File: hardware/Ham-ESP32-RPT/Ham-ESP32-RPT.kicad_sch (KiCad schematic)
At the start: 17 parts, among them J1 USB_C_Receptacle_USB2.0_16P, U1 ESP32-S3-WROOM-1, U2 D3V3XA4B10LP, U3 TLV75801PDBV

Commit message: Mise à jour documents
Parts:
- added J2: Conn_Coaxial, Connector_Coaxial:SMA_Molex_73251-1153_EdgeMount_Horizontal, symbol Connector:Conn_Coaxial
- added U4: ESP32-S3-DevKitC, PCM_Espressif:ESP32-S3-DevKitC, symbol PCM_Espressif:ESP32-S3-DevKitC
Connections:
- new net: U4.1 (3V3), U4.2 (3V3)
- new net: U4.22 (GND), U4.23 (GND), U4.24 (GND), U4.44 (GND)
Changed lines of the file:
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@@
+	)
+	(symbol
+		(lib_id "Connector:Conn_Coaxial")
+		(at 205.74 127 0)
+		(unit 1)
+		(exclude_from_sim no)
+		(in_bom yes)
+		(on_board yes)
+		(dnp no)
+		(fields_autoplaced yes)
+		(property "Reference" "J2"
+			(at 209.55 126.0231 0)
+			(effects
+				(font
+					(size 1.27 1.27)
+				)
+				(justify left)
+			)
+		)
+		(property "Value" "Conn_Coaxial"
+			(at 209.55 128.5631 0)
+			(effects
+				(font
+					(size 1.27 1.27)
+				)
+				(justify left)
+			)
+		)
+		(property "Footprint" "Connector_Coaxial:SMA_Molex_73251-1153_EdgeMount_Horizontal"
+			(at 205.74 127 0)
+			(effects
+				(font
+					(size 1.27 1.27)
+				)
+				(hide yes)
+			)
+		)
+		(property "Datasheet" "~"
+			(at 205.74 127 0)
+			(effects
+				(font
+					(size 1.27 1.27)
+				)
+				(hide yes)
+			)
+		)
+		(property "Description" "coaxial connector (BNC, SMA, SMB, SMC, Cinch/RCA, LEMO, ...)"
+			(at 205.74 127 0)
+			(effects
+				(font
+					(size 1.27 1.27)
+				)
+				(hide yes)
+			)
+		)
+		(pin "2"
+		)
+		(pin "1"
+		)
+		(instances
+			(project ""
+				(path "/1aedab51-3492-4fbd-b88f-5a8cb3ade46f"
+					(reference "J2")
+					(unit 1)
+				)
+			)
+		)
 	)
 	(symbol
@@
 					(unit 1)
 				)
+			)
+		)
+	)
+	(symbol
+		(lib_id "PCM_Espressif:ESP32-S3-DevKitC")
+		(at 251.46 104.14 0)
+		(unit 1)
+		(exclude_from_sim no)
+		(in_bom yes)
+		(on_board yes)
+		(dnp no)
+		(fields_autoplaced yes)
+		(property "Reference" "U4"
+			(at 253.6541 149.86 0)
+			(effects
+				(font
+					(size 1.27 1.27)
+				)
+				(justify left)
+			)
+		)
+		(property "Value" "ESP32-S3-DevKitC"
+			(at 253.6541 152.4 0)
+			(effects
+				(font
+					(size 1.27 1.27)
+				)
+				(justify left)
+			)
+		)
+		(property "Footprint" "PCM_Espressif:ESP32-S3-DevKitC"
+			(at 251.46 161.29 0)
+			(effects
+				(font
+					(size 1.27 1.27)
+				)
+				(hide yes)
+			)
+		)
+		(property "Datasheet" ""
+			(at 191.77 106.68 0)
+			(effects
+				(font
+					(size 1.27 1.27)
+				)
+				(hide yes)
+			)
+		)
+		(property "Description" "ESP32-S3-DevKitC"
+			(at 251.46 104.14 0)
+			(effects
+				(font
+					(size 1.27 1.27)
+				)
+				(hide yes)
+			)
+		)
+		(pin "14"
+		)
+		(pin "20"
+		)
+		(pin "11"
+		)
+		(pin "31"
+		)
+		(pin "38"
+		)
+		(pin "19"
+		)
+		(pin "39"
+		)
+		(pin "1"
+		)
+		(pin "42"
+		)
+		(pin "13"
+		)
+		(pin "21"
+		)
+		(pin "22"
+		)
+		(pin "32"
+		)
+		(pin "44"
+		)
+		(pin "25"
+		)
+		(pin "33"
+		)
+		(pin "26"
+		)
+		(pin "34"
+		)
+		(pin "35"
+		)
+		(pin "28"
+		)
+		(pin "36"
+		)
+		(pin "18"
+		)
+		(pin "3"
+		)
+		(pin "27"
+		)
+		(pin "2"
+		)
+		(pin "23"
+		)
+		(pin "17"
+		)
+		(pin "16"
+		)
+		(pin "37"
+		)
+		(pin "41"
+		)
+		(pin "5"
+		)
+		(pin "29"
+		)
+		(pin "6"
+		)
+		(pin "8"
+		)
+		(pin "24"
+		)
+		(pin "10"
+		)
+		(pin "43"
+		)
+		(pin "15"
+		)
+		(pin "40"
+		)
+		(pin "30"
+		)
+		(pin "7"
+		)
+		(pin "9"
+		)
+		(pin "12"
+		)
+		(pin "4"
+		)
+		(instances
+			(project ""
+				(path "/1aedab51-3492-4fbd-b88f-5a8cb3ade46f"
+					(reference "U4")
+					(unit 1)
+				)

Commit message: doc HAM-ESP32
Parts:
- removed BOOT1, RESET1: SW_MEC_5E, Button_Switch_SMD:SW_MEC_5GSH9, symbol PCM_Switch:SW_MEC_5E
- removed C1, C3, C4: 0.1µF, Capacitor_SMD:C_0805_2012Metric, symbol Device:C
- removed C2, C6, C7: 10µF, Capacitor_SMD:C_0805_2012Metric, symbol Device:C
- removed J1: USB_C_Receptacle_USB2.0_16P, Connector_USB:USB_C_Receptacle_GCT_USB4085, symbol Connector:USB_C_Receptacle_USB2.0_16P
- removed J2: Conn_Coaxial, Connector_Coaxial:SMA_Molex_73251-1153_EdgeMount_Horizontal, symbol Connector:Conn_Coaxial
- removed R3: 10k, Resistor_SMD:R_0805_2012Metric, symbol Device:R
- removed R6: 1M, Resistor_SMD:R_0805_2012Metric, symbol Device:R
- removed R7: 200k, Resistor_SMD:R_0805_2012Metric, symbol Device:R
- removed R8: 5.1K, Resistor_SMD:R_0805_2012Metric, symbol Device:R
- removed U1: ESP32-S3-WROOM-1, RF_Module:ESP32-S3-WROOM-1U, symbol RF_Module:ESP32-S3-WROOM-1
- removed U2: D3V3XA4B10LP, Package_DFN_QFN:Diodes_UDFN-10_1.0x2.5mm_P0.5mm, symbol Power_Protection:D3V3XA4B10LP
- removed U3: TLV75801PDBV, Package_TO_SOT_SMD:SOT-23-5, symbol Regulator_Linear:TLV75801PDBV
- added D1: GREEN, symbol Device:LED
- added J1: RSSI IN, symbol Connector:Conn_01x02_Pin
- added J2: AUDIO OUT, symbol Connector:Conn_01x02_Pin
- added J3: AUDIO IN, symbol Connector:Conn_01x02_Pin
- added J4: PTT OUT, symbol Connector:Conn_01x02_Pin
- added R1, R2: 330R, symbol Device:R
- added SW1: REP TEST, symbol Switch:SW_Push
- added U1: CS5343, Package_SO:TSSOP-10_3x3mm_P0.5mm, symbol Audio:CS5343
- added U2: CS4344, Package_SO:TSSOP-10_3x3mm_P0.5mm, symbol Audio:CS4344
- D2: value LED -> RED; footprint LED_SMD:LED_0805_2012Metric -> (none)
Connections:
- net GND: now also U4.22 (GND), U4.23 (GND), U4.24 (GND), U4.44 (GND), D1.1 (K), J1.2 (Pin_2), J2.2 (Pin_2), J3.2 (Pin_2), J4.2 (Pin_2), SW1.2, U1.9 (GND), U2.8 (GND)
- net at D2.2 (A): now also R2.2
- net VCC: now reaches U4.1 (3V3), U4.2 (3V3)
- net VCC: now also U1.10 (VA), U2.9 (VA)
- net at U4.12 (GPIO8/ADC1_CH7): now also J1.1 (Pin_1)
- net at U4.13 (GPIO3/ADC1_CH2): now also U1.1 (SDOUT)
- net at U4.15 (GPIO9/ADC1_CH8): now also R1.1
- net at U4.16 (GPIO10/ADC1_CH9): now also R2.1
- net at U4.17 (GPIO11/ADC2_CH0): now also SW1.1
- net at U4.18 (GPIO12/ADC2_CH1): now also J4.1 (Pin_1)
- net at U4.31 (GPIO0): now also U1.4 (MCLK)
- net at U4.4 (GPIO4/ADC1_CH3): now also U2.4 (MCLK)
- net at U4.40 (GPIO2/ADC1_CH1): now also U1.2 (SCLK)
- net at U4.41 (GPIO1/ADC1_CH0): now also U1.3 (LRCK)
- net at U4.5 (GPIO5/ADC1_CH4): now also U2.3 (LRCK)
- net at U4.6 (GPIO6/ADC1_CH5): now also U2.2 (~{DEM}/SCLK)
- net at U4.7 (GPIO7/ADC1_CH6): now also U2.1 (SDIN)
- new net: J3.1 (Pin_1), U1.5 (FILT+)
- new net: J2.1 (Pin_1), U2.7 (AOUTL)
- new net: D1.2 (A), R1.2
- no-connect marks 2 -> 0
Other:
- moved on the sheet: U4

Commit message: Update Kicad Schematic
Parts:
- removed J1: RSSI IN, symbol Connector:Conn_01x02_Pin
- removed J2: AUDIO OUT, symbol Connector:Conn_01x02_Pin
- removed J3: AUDIO IN, symbol Connector:Conn_01x02_Pin
- removed J4: PTT OUT, symbol Connector:Conn_01x02_Pin
- removed U1: CS5343, Package_SO:TSSOP-10_3x3mm_P0.5mm, symbol Audio:CS5343
- removed U2: CS4344, Package_SO:TSSOP-10_3x3mm_P0.5mm, symbol Audio:CS4344
- added FB1: FerriteBead, Ferrite_THT:LairdTech_28C0236-0JW-10, symbol Device:FerriteBead
- added J5: Conn_01x04_Socket, Connector_JST:JST_XH_B4B-XH-A_1x04_P2.50mm_Vertical, symbol Connector:Conn_01x04_Socket
- added Q1: MMBT3904, Package_TO_SOT_SMD:SOT-23, symbol Transistor_BJT:MMBT3904
- D1, D2: footprint (none) -> LED_SMD:LED_1206_3216Metric
- R1, R2: footprint (none) -> Resistor_SMD:R_1206_3216Metric
- SW1: footprint (none) -> Button_Switch_THT:SW_PUSH_6mm

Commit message: PCB kicad update
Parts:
- removed J5: Conn_01x04_Socket, Connector_JST:JST_XH_B4B-XH-A_1x04_P2.50mm_Vertical, symbol Connector:Conn_01x04_Socket
- removed Q1: MMBT3904, Package_TO_SOT_SMD:SOT-23, symbol Transistor_BJT:MMBT3904
- removed SW1: REP TEST, Button_Switch_THT:SW_PUSH_6mm, symbol Switch:SW_Push
- removed U4: ESP32-S3-DevKitC, PCM_Espressif:ESP32-S3-DevKitC, symbol PCM_Espressif:ESP32-S3-DevKitC
- added D1: BLUE, LED_SMD:LED_1206_3216Metric, symbol Device:LED
- added F1: 2A, Fuse:Fuse_1206_3216Metric, symbol Device:Fuse
- added F2, F3: 4A, Fuse:Fuse_1206_3216Metric, symbol Device:Fuse
- added FB2, FB3, FB4: VK200, Inductor_SMD:L_Neosid_MicroCoil_Ms36-L, symbol Device:FerriteBead
- added J1: 5V SUPPLY, Connector_JST:JST_XH_B2B-XH-A_1x02_P2.50mm_Vertical, symbol Connector_Generic:Conn_01x02
- added J2: 12V SUPPLY, Connector_JST:JST_XH_B2B-XH-A_1x02_P2.50mm_Vertical, symbol Connector_Generic:Conn_01x02
- added J3: RX RADIO, Connector_JST:JST_XH_B5B-XH-A_1x05_P2.50mm_Vertical, symbol Connector_Generic:Conn_01x05
- added J4: TX RADIO, Connector_JST:JST_XH_B4B-XH-A_1x04_P2.50mm_Vertical, symbol Connector_Generic:Conn_01x04
- added J5: AUX BTN LED, Connector_JST:JST_XH_B5B-XH-A_1x05_P2.50mm_Vertical, symbol Connector_Generic:Conn_01x05
- added J6: SPEAKER, Connector_JST:JST_XH_B2B-XH-A_1x02_P2.50mm_Vertical, symbol Connector_Generic:Conn_01x02
- added Q1: MMBT2222A, Package_TO_SOT_SMD:TSOT-23, symbol Transistor_BJT:MMBT2222A
- added R1: 330R, Resistor_SMD:R_1206_3216Metric, symbol Device:R
- added R2: 3.3K, Resistor_SMD:R_1206_3216Metric, symbol Device:R
- added SW2: TEST, Button_Switch_SMD:SW_Push_1P1T_NO_E-Switch_TL3301NxxxxxG, symbol Switch:SW_Push
- added U1: ESP32-S3-DevKitC-V2, Ham-ESP32-RPT-pretty:ESP32-S3-DevKitC-V2, symbol Ham-ESP32-RPT:ESP32-S3-DevKitC-V2
- added U2: PmodI2S2, symbol Ham-ESP32-RPT:PmodI2S2
- added U3: INA219AxD, Package_SO:SOIC-8_3.9x4.9mm_P1.27mm, symbol Sensor_Energy:INA219AxD
- added VR1, VR2, VR3: 10K, Potentiometer_SMD:Potentiometer_Bourns_3314R-1_Vertical_Hole, symbol Device:R_Potentiometer
- FB1: value FerriteBead -> VK200; footprint Ferrite_THT:LairdTech_28C0236-0JW-10 -> Inductor_SMD:L_Neosid_MicroCoil_Ms36-L
- renumbered D1 to D3, R2 to R3, R1 to R4
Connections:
- net GND: now also J1.2 (Pin_2), J2.2 (Pin_2), J3.4 (Pin_4), J4.3 (Pin_3), Q1.2 (E), R1.2, SW2.2, U1.1 (GND), U1.42 (GND), U2.11 (GND), U2.14 (A_IN-), U2.16 (A_OUT-), U2.5 (GND), U3.6 (GND), VR1.1, VR2.3, VR3.1
- net at R4.1: now also U1.8 (G15)
- net at R3.1: now also U1.24 (G14)
- net at FB1.1: now also D1.2 (A), F1.2
- net +5V: now reaches FB1.2
- net +5V: now also U1.22 (5V)
- new net: R2.1, U1.20 (G12)
- new net: Q1.1 (B), R2.2
- new net: U2.13 (A_IN+), VR1.2
- new net: FB2.2, VR1.3
- new net: D1.1 (K), R1.1
- new net: FB4.1, J3.1 (Pin_1)
- new net: FB2.1, J3.2 (Pin_2)
- new net: F2.2, J3.5 (Pin_5)
- new net: F1.1, J1.1 (Pin_1)
- new net: U1.12 (G8), U3.3 (SDA)
- new net: U1.15 (G3), U2.4 (ADOUT_SDIN)
- new net: U1.17 (G9), U3.4 (SCL)
- new net: SW2.1, U1.19 (G11)
- new net: U1.29 (G0), U2.1 (ADOUT_MCLK)
- new net: U1.4 (G4), U2.7 (ADIN_MCLK)
- new net: U1.40 (G2), U2.3 (ADOUT_SCLK)
- new net: U1.41 (G1), U2.2 (ADOUT_LRCK)
- new net: U1.5 (G5), U2.8 (ADIN_LRCK)
- new net: U1.6 (G6), U2.9 (ADIN_SCLK)
- new net: U1.7 (G7), U2.10 (ADIN_SDOUT)
- new net: J4.1 (Pin_1), Q1.3 (C)
- new net: FB3.2, J4.2 (Pin_2)
- new net: F3.2, J4.4 (Pin_4)
- new net: U2.15 (A_OUT+), VR2.1
- new net: FB4.2, VR3.3
- new net: FB3.1, VR2.2
- new net: F2.1, F3.1, J2.1 (Pin_1)
- new net: U3.8 (IN+), VR3.2
- new net +3.3V: U1.2 (3V3), U1.21 (3V3), U2.12 (3V3), U2.6 (3V3), U3.5 (VS)
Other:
- moved on the sheet: D2, D3, FB1, R3, R4

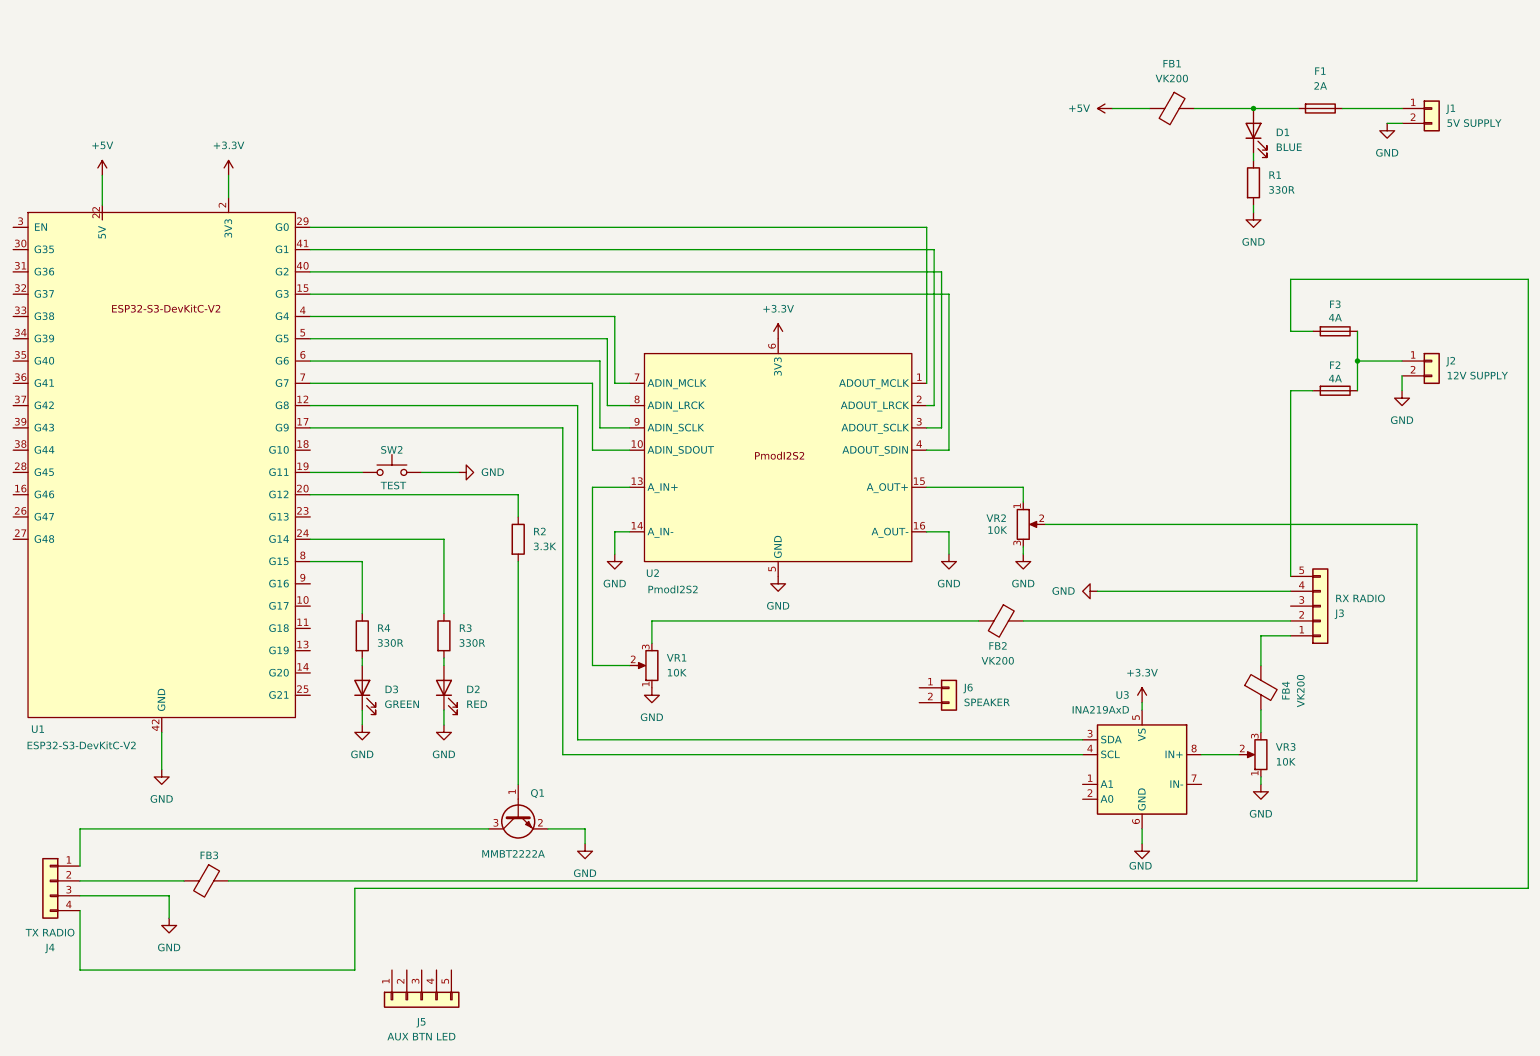
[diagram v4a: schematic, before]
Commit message: Add Vk200 footprint
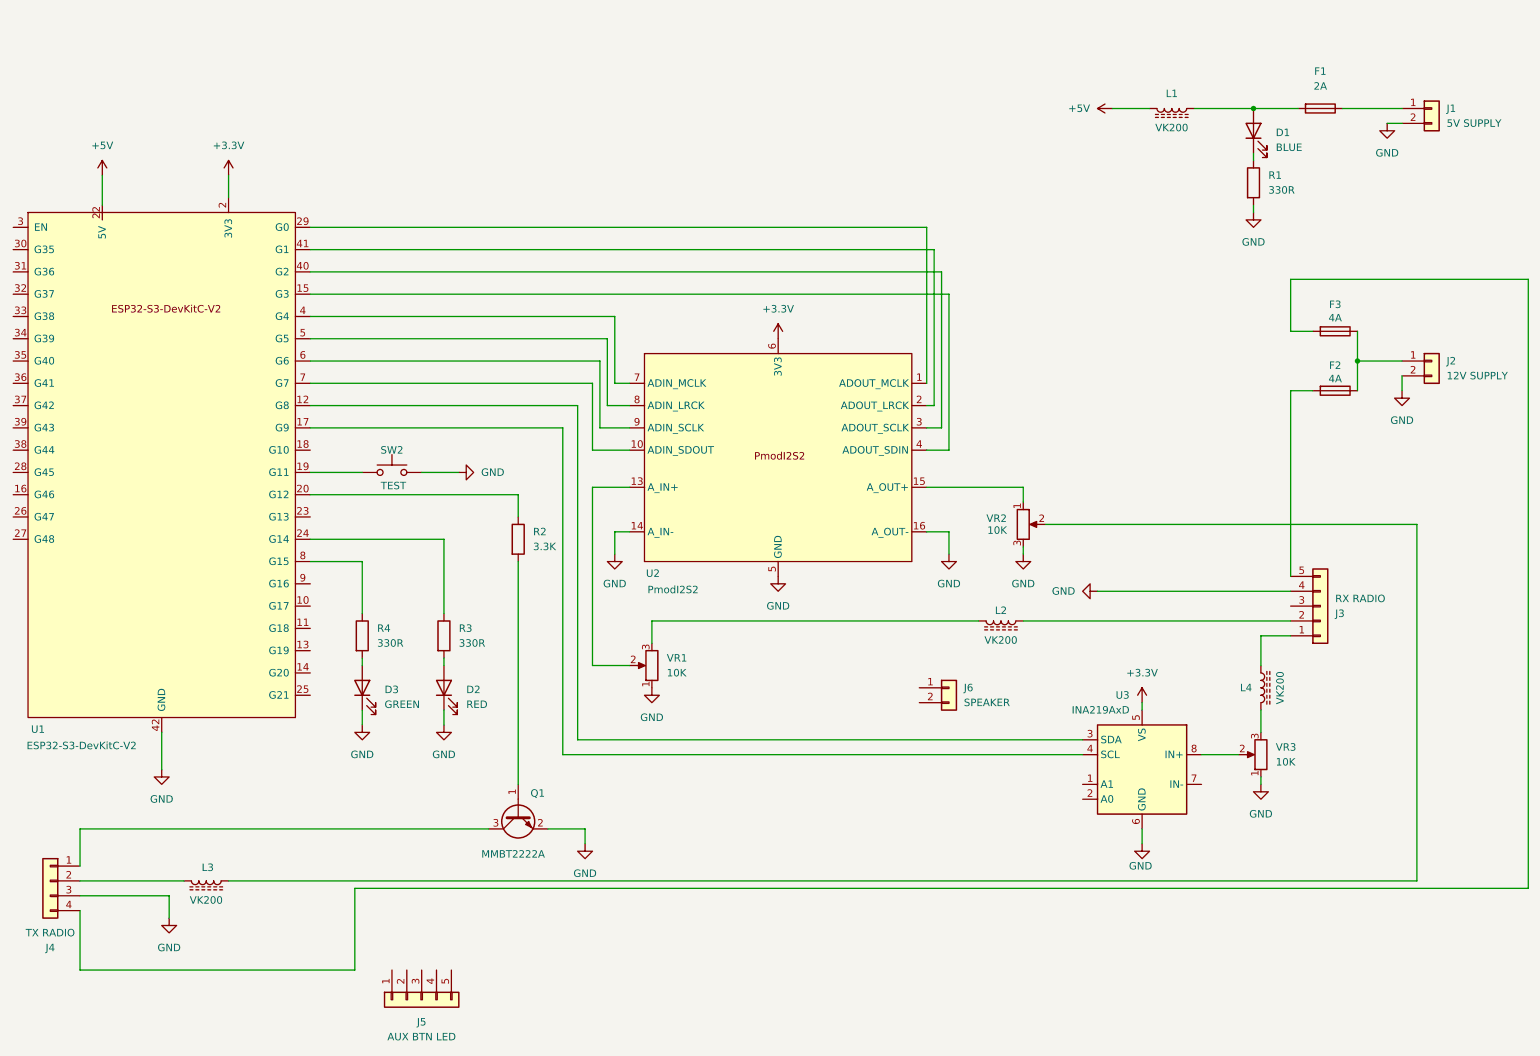
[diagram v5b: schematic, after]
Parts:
- L1: renamed from FB1; footprint Inductor_SMD:L_Neosid_MicroCoil_Ms36-L -> Ham-ESP32-RPT-pretty:VK200; symbol Device:FerriteBead -> Ham-ESP32-RPT:VK200
- L2: renamed from FB2; footprint Inductor_SMD:L_Neosid_MicroCoil_Ms36-L -> Ham-ESP32-RPT-pretty:VK200; symbol Device:FerriteBead -> Ham-ESP32-RPT:VK200
- L3: renamed from FB3; footprint Inductor_SMD:L_Neosid_MicroCoil_Ms36-L -> VK200; symbol Device:FerriteBead -> Ham-ESP32-RPT:VK200
- L4: renamed from FB4; footprint Inductor_SMD:L_Neosid_MicroCoil_Ms36-L -> Ham-ESP32-RPT-pretty:VK200; symbol Device:FerriteBead -> Ham-ESP32-RPT:VK200
- Q1: footprint Package_TO_SOT_SMD:TSOT-23 -> Package_TO_SOT_SMD:SOT-23
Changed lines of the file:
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@@
 	)
 	(symbol
-		(lib_id "Device:FerriteBead")
+		(lib_id "Ham-ESP32-RPT:VK200")
 		(at 236.22 129.54 0)
 		(unit 1)
@@
 		(on_board yes)
 		(dnp no)
-		(property "Reference" "FB4"
-			(at 240.538 130.048 90)
+		(property "Reference" "L4"
+			(at 233.68 129.54 0)
 			(effects
 				(font
@@
 		)
 		(property "Value" "VK200"
-			(at 243.078 130.048 90)
-			(effects
-				(font
-					(size 1.27 1.27)
-				)
-			)
-		)
-		(property "Footprint" "Inductor_SMD:L_Neosid_MicroCoil_Ms36-L"
-			(at 234.442 129.54 90)
+			(at 239.522 129.54 90)
+			(effects
+				(font
+					(size 1.27 1.27)
+				)
+			)
+		)
+		(property "Footprint" "Ham-ESP32-RPT-pretty:VK200"
+			(at 236.22 129.54 0)
 			(effects
 				(font
@@
 			)
 		)
-		(property "Description" "Ferrite bead"
+		(property "Description" "Inductor with ferrite core"
 			(at 236.22 129.54 0)
 			(effects
@@
 			(project "Ham-ESP32-RPT"
 				(path "/1aedab51-3492-4fbd-b88f-5a8cb3ade46f"
-					(reference "FB4")
+					(reference "L4")
 					(unit 1)
 				)
@@
 	)
 	(symbol
-		(lib_id "Device:FerriteBead")
+		(lib_id "Ham-ESP32-RPT:VK200")
 		(at 191.77 118.11 270)
 		(unit 1)
@@
 		(on_board yes)
 		(dnp no)
-		(property "Reference" "FB2"
-			(at 191.262 122.428 90)
+		(property "Reference" "L2"
+			(at 191.77 116.332 90)
 			(effects
 				(font
@@
 		)
 		(property "Value" "VK200"
-			(at 191.262 124.968 90)
-			(effects
-				(font
-					(size 1.27 1.27)
-				)
-			)
-		)
-		(property "Footprint" "Inductor_SMD:L_Neosid_MicroCoil_Ms36-L"
-			(at 191.77 116.332 90)
+			(at 191.77 121.412 90)
+			(effects
+				(font
+					(size 1.27 1.27)
+				)
+			)
+		)
+		(property "Footprint" "Ham-ESP32-RPT-pretty:VK200"
+			(at 191.77 118.11 0)
 			(effects
 				(font
@@
 			)
 		)
-		(property "Description" "Ferrite bead"
+		(property "Description" "Inductor with ferrite core"
 			(at 191.77 118.11 0)
 			(effects
@@
 			(project "Ham-ESP32-RPT"
 				(path "/1aedab51-3492-4fbd-b88f-5a8cb3ade46f"
-					(reference "FB2")
+					(reference "L2")
 					(unit 1)
 				)
@@
 	)
 	(symbol
-		(lib_id "Device:FerriteBead")
+		(lib_id "Ham-ESP32-RPT:VK200")
 		(at 55.88 162.56 270)
 		(unit 1)
@@
 		(on_board yes)
 		(dnp no)
-		(property "Reference" "FB3"
-			(at 56.388 158.242 90)
+		(property "Reference" "L3"
+			(at 56.134 160.274 90)
 			(effects
 				(font
@@
 		)
 		(property "Value" "VK200"
-			(at 56.896 156.21 90)
-			(effects
-				(font
-					(size 1.27 1.27)
-				)
-				(hide yes)
-			)
-		)
-		(property "Footprint" "Inductor_SMD:L_Neosid_MicroCoil_Ms36-L"
-			(at 55.88 160.782 90)
+			(at 55.88 165.862 90)
+			(effects
+				(font
+					(size 1.27 1.27)
+				)
+			)
+		)
+		(property "Footprint" "VK200"
+			(at 55.88 162.56 0)
 			(effects
 				(font
@@
 			)
 		)
-		(property "Description" "Ferrite bead"
+		(property "Description" "Inductor with ferrite core"
 			(at 55.88 162.56 0)
 			(effects
@@
 			(project "Ham-ESP32-RPT"
 				(path "/1aedab51-3492-4fbd-b88f-5a8cb3ade46f"
-					(reference "FB3")
+					(reference "L3")
 					(unit 1)
 				)
@@
 			)
 		)
-		(property "Footprint" "Package_TO_SOT_SMD:TSOT-23"
+		(property "Footprint" "Package_TO_SOT_SMD:SOT-23"
 			(at 111.125 156.21 0)
 			(effects
@@
 		)
 		(property "Description" "600mA Ic, 40V Vce, NPN Transistor, SOT-23"
+			(at 109.22 151.13 0)
+			(effects
+				(font
+					(size 1.27 1.27)
+				)
+				(hide yes)
+			)
+		)
+		(property "Sim.Device" "NPN"
+			(at 109.22 151.13 0)
+			(effects
+				(font
+					(size 1.27 1.27)
+				)
+				(hide yes)
+			)
+		)
+		(property "Sim.Pins" "1=B 2=E 3=C"
 			(at 109.22 151.13 0)
 			(effects
@@
 	)
 	(symbol
-		(lib_id "Device:FerriteBead")
+		(lib_id "Ham-ESP32-RPT:VK200")
 		(at 220.98 30.48 270)
 		(unit 1)
@@
 		(on_board yes)
 		(dnp no)
-		(fields_autoplaced yes)
-		(property "Reference" "FB1"
-			(at 221.0308 22.86 90)
+		(property "Reference" "L1"
+			(at 220.98 27.94 90)
 			(effects
 				(font
@@
 		)
 		(property "Value" "VK200"
-			(at 221.0308 25.4 90)
-			(effects
-				(font
-					(size 1.27 1.27)
-				)
-			)
-		)
-		(property "Footprint" "Inductor_SMD:L_Neosid_MicroCoil_Ms36-L"
-			(at 220.98 28.702 90)
+			(at 220.98 33.782 90)
+			(effects
+				(font
+					(size 1.27 1.27)
+				)
+			)
+		)
+		(property "Footprint" "Ham-ESP32-RPT-pretty:VK200"
+			(at 220.98 30.48 0)
 			(effects
 				(font
@@
 			)
 		)
-		(property "Description" "Ferrite bead"
+		(property "Description" "Inductor with ferrite core"
 			(at 220.98 30.48 0)
 			(effects
@@
 			(project ""
 				(path "/1aedab51-3492-4fbd-b88f-5a8cb3ade46f"
-					(reference "FB1")
-					(unit 1)
-				)
+					(reference "L1")
+					(unit 1)
+				)
